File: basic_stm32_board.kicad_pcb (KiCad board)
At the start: 4 copper layers, 46.2 x 44.7 mm, 61 parts, among them J1 Screw_Terminal_01x02, J2 USB_B_Micro, J3 Conn_01x04, J4 Conn_01x04, J5 Conn_ARM_JTAG_SWD_10, Q1 AO3401A, SW1 SW_SPDT, U1 STM32F405RGT6, U2 MP2303ADN, U3 USBLC6-2SC6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

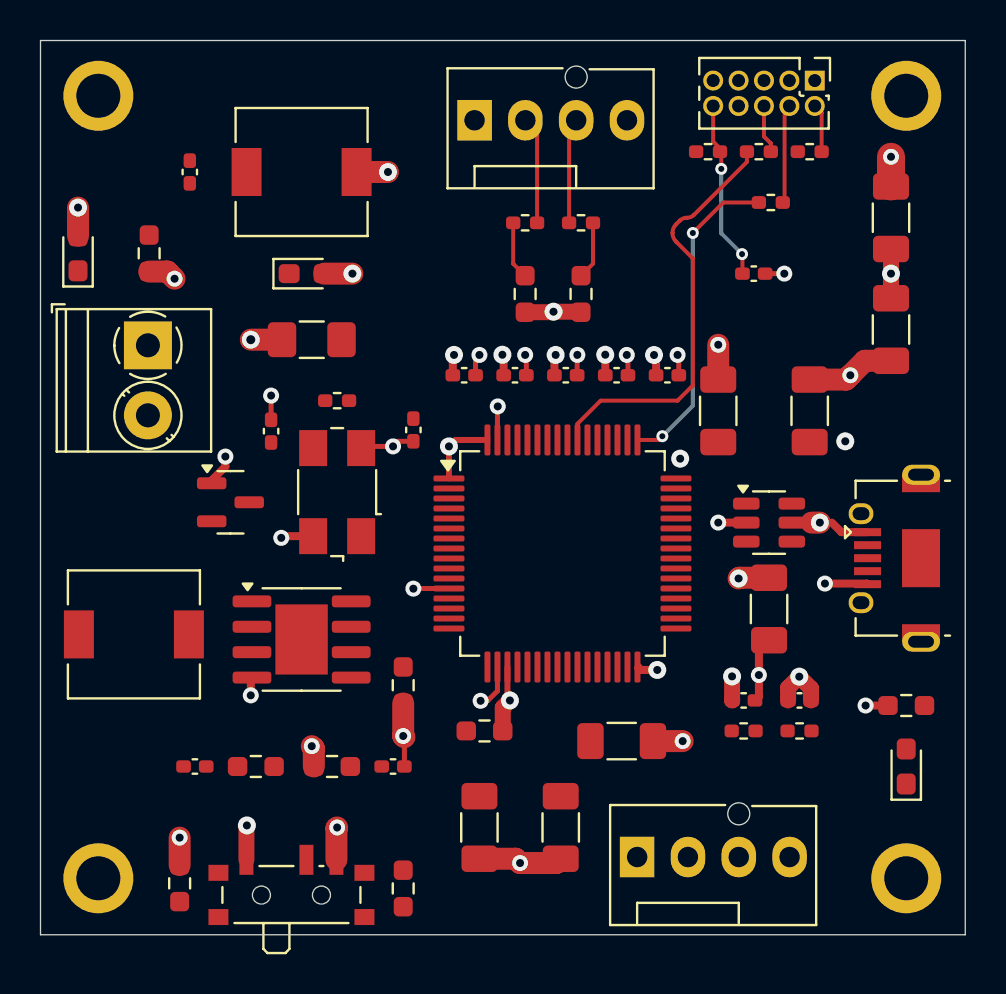
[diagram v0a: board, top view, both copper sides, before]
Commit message: Removed all traces
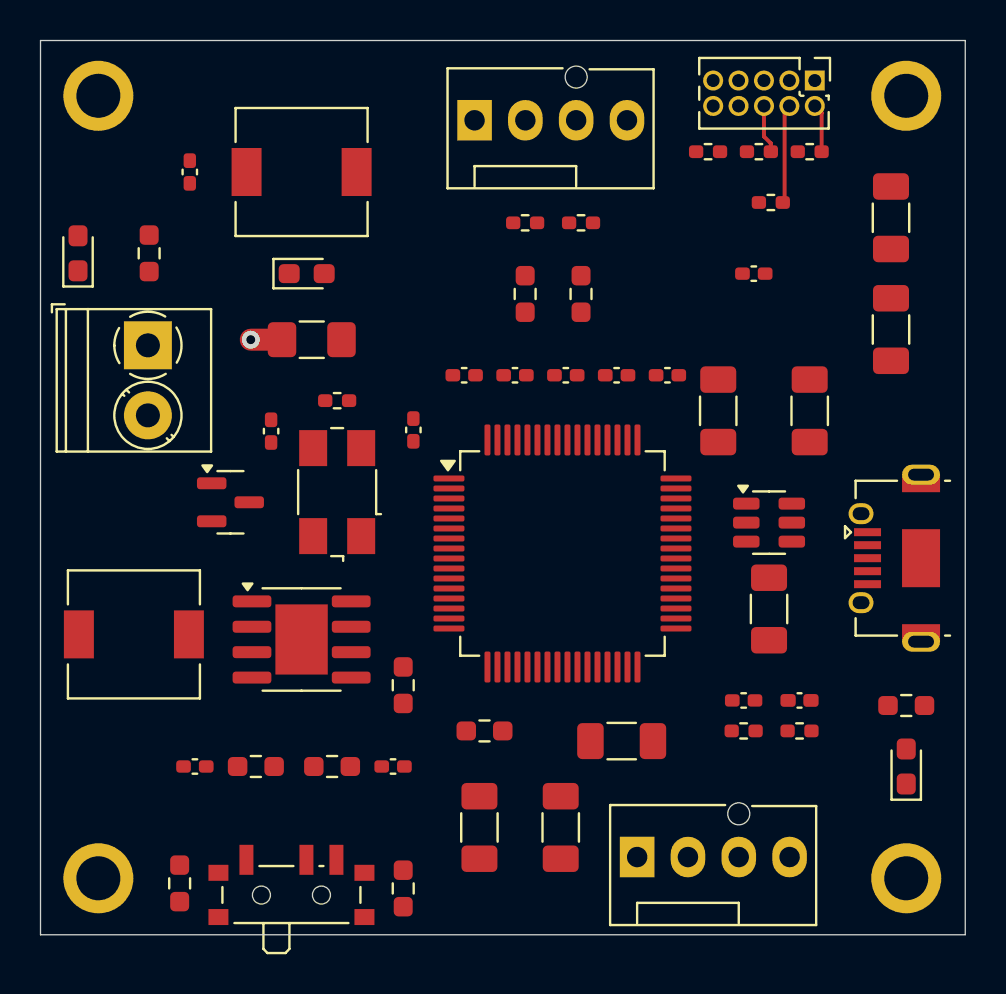
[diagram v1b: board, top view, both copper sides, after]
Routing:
- net GND: track 50.2 -> 0.00 mm, vias 28 -> 0
- net +3.3VA: track 33.6 -> 0.00 mm, vias 20 -> 0
- net SWO: track 21.2 -> 0.00 mm
- net SWCLK: track 16.0 -> 0.00 mm, vias 2 -> 0
- net Net-(J5-~{RESET}): track 8.99 -> 0.00 mm, vias 2 -> 0
- net Net-(J3-Pin_3): track 5.27 -> 0.00 mm
- net Net-(J3-Pin_2): track 5.37 -> 0.83 mm
- net I2C1_SDA: track 2.89 -> 0.00 mm
- net I2C1_SCL: track 2.89 -> 0.00 mm
